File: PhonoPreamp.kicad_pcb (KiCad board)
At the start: 2 copper layers, 100 x 100 mm, 101 parts, among them J1 Conn_01x03, J2 Conn_01x02, J3 Conn_01x02, J4 Conn_01x02, J5 Conn_01x02, J6 Conn_01x01, J7 Conn_01x01, J8 Conn_01x01, J9 Conn_01x01, Q1 2N5551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

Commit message: Made some space around capacitors
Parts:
- moved C26 5.27 mm to (117.2, 110.0)
- moved C15 4.14 mm to (116.2, 45.6)
- moved C25 3.67 mm to (112.7, 110.0)
- moved C16 3.40 mm to (112.0, 45.5)
- moved R39 3.26 mm to (106.0, 41.2)
- moved C12 2.69 mm to (107.5, 45.5)
- moved C24 2.47 mm to (108.2, 110.0)
- moved C13 2.07 mm to (103.2, 45.6)
- moved R40 1.88 mm to (106.2, 105.8)
- moved C14 1.75 mm to (98.7, 45.6)
- moved R36 1.70 mm to (117.0, 119.7)
- moved R35 1.55 mm to (116.7, 122.8)
- moved R33 1.55 mm to (106.8, 122.8)
- moved R34 1.46 mm to (106.8, 119.7)
- moved C23 1.15 mm to (103.8, 110.0)
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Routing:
- net Net-(C12-Pad2): track 29.3 -> 35.4 mm
- net Net-(C22-Pad2): track 30.8 -> 36.2 mm
- net GNDS1: track 148.9 -> 152.7 mm
- net GNDS2: track 239.0 -> 242.1 mm
- net Net-(R39-Pad1): track 30.3 -> 28.6 mm
- net Net-(C28-Pad2): track 21.2 -> 19.7 mm
- net Net-(C15-Pad2): track 8.12 -> 9.35 mm
- net Net-(R40-Pad1): track 115.7 -> 116.8 mm
- net Net-(C29-Pad2): track 19.3 -> 18.6 mm
- net Net-(C25-Pad2): track 8.98 -> 9.49 mm

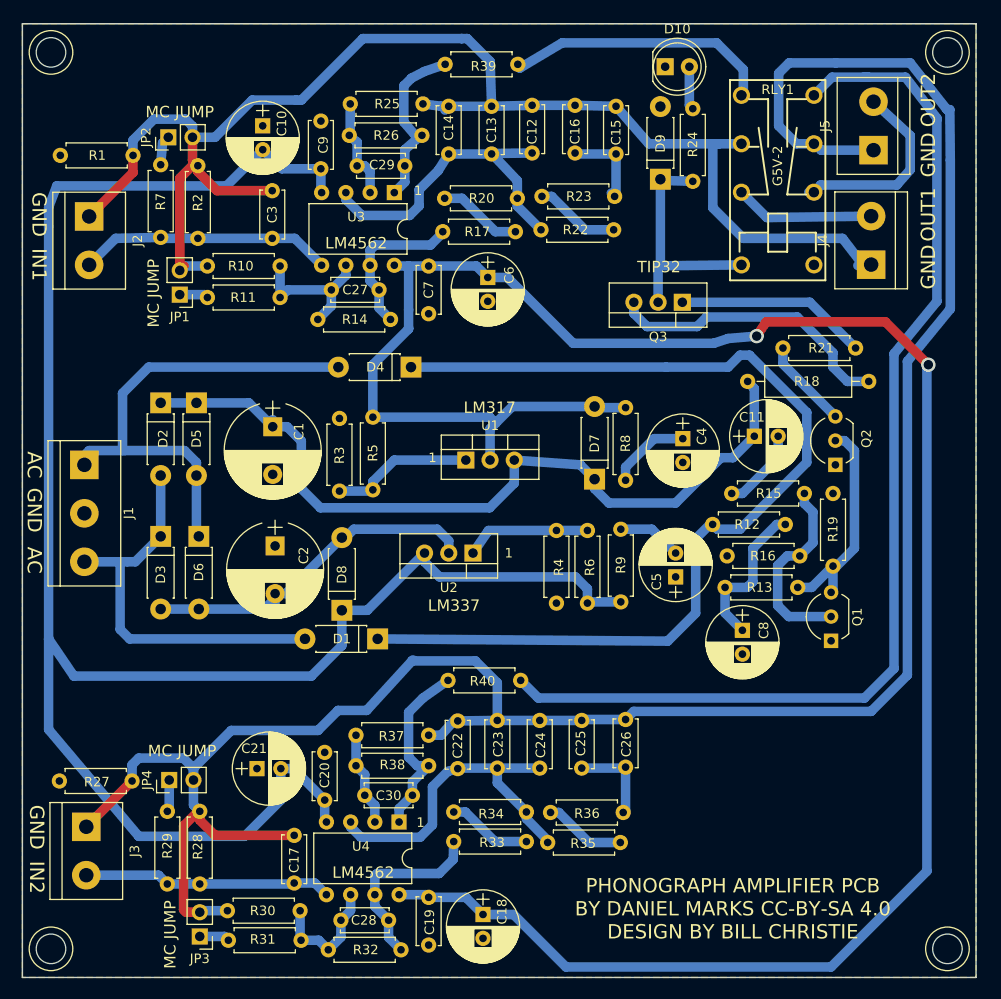
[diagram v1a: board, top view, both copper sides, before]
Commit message: Bigger capacitor footprints
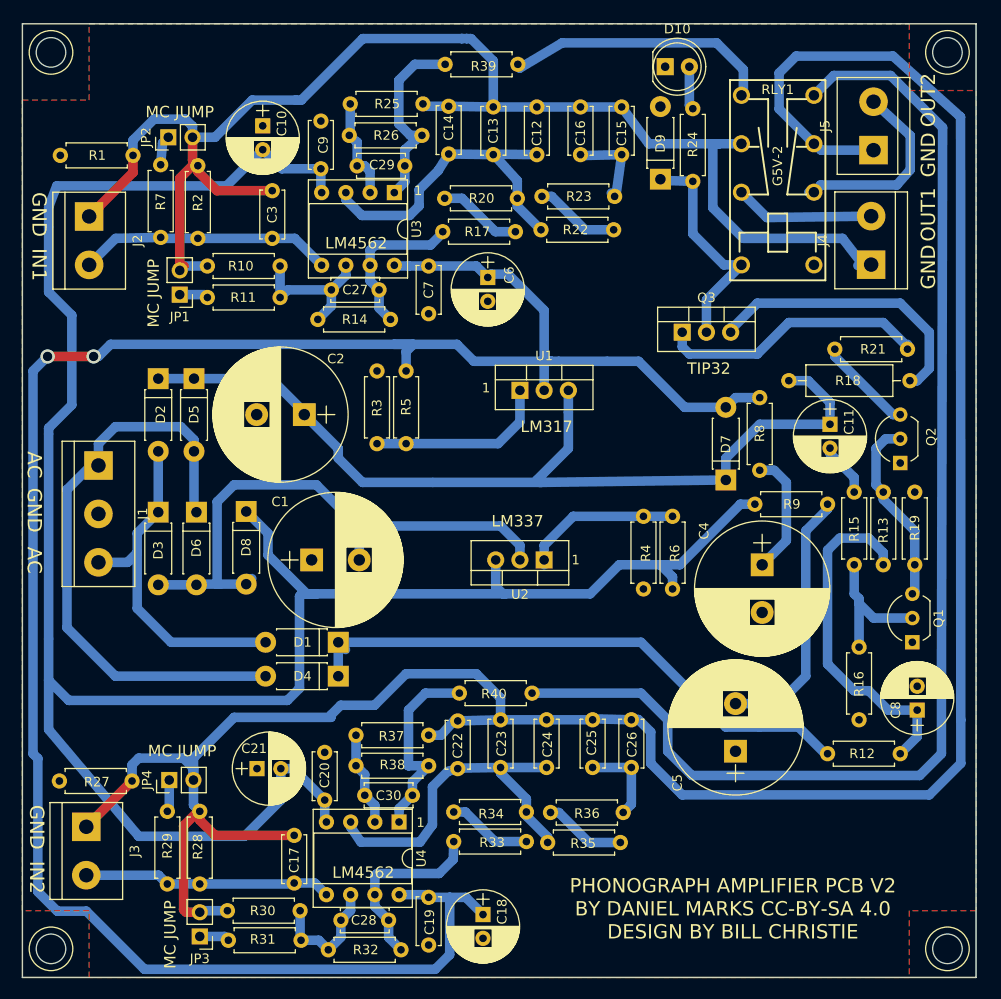
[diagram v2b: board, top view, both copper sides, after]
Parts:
- C1, C2: footprint Capacitors_THT:CP_Radial_D10.0mm_P5.00mm -> Capacitors_THT:CP_Radial_D14.0mm_P5.00mm
- C4, C5: footprint Capacitors_THT:CP_Radial_D7.5mm_P2.50mm -> Capacitors_THT:CP_Radial_D14.0mm_P5.00mm
- U3, U4: footprint Housings_DIP:DIP-8_W7.62mm -> Housings_DIP:DIP-8_W7.62mm_Socket
- moved D4 33.3 mm to (87.1, 105.4)
- moved R12 26.9 mm to (146.1, 113.5)
- moved R16 22.1 mm to (141.7, 110.0), turned to 90 degrees
- moved R9 21.8 mm to (138.4, 87.4), turned to 180 degrees
- moved C8 20.1 mm to (147.8, 109.0), turned to 90 degrees
- moved C5 19.3 mm to (128.8, 113.3)
- moved C4 15.6 mm to (131.6, 93.7)
- moved D8 14.4 mm to (77.5, 88.1), turned to 270 degrees
- moved R8 14.1 mm to (131.3, 76.2)
- moved D7 13.8 mm to (127.8, 84.8)
- moved R13 13.4 mm to (144.3, 86.1), turned to 270 degrees
- moved U1 9.25 mm to (106.2, 75.4)
- moved R4 9.25 mm to (119.1, 96.3)
- moved R15 9.12 mm to (141.2, 93.7), turned to 90 degrees
- moved R6 9.05 mm to (122.2, 96.3)
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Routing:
- net Net-(D1-Pad1): track 107.5 -> 60.8 mm
- net -15V: track 206.5 -> 243.4 mm
- net Net-(C2-Pad2): track 36.8 -> 60.2 mm
- net Net-(C5-Pad2): track 6.79 -> 27.5 mm
- net Net-(C8-Pad1): track 16.9 -> 36.9 mm
- net GNDS2: track 242.1 -> 259.9 mm
- net Net-(R40-Pad1): track 116.8 -> 131.7 mm
- net Net-(C1-Pad1): track 85.5 -> 98.4 mm
- net Net-(D4-Pad2): track 51.1 -> 63.1 mm
- net Net-(Q3-Pad1): track 20.2 -> 28.6 mm
- net Net-(Q1-Pad2): track 20.7 -> 15.1 mm
- net Net-(D1-Pad2): track 42.4 -> 37.2 mm
- net Net-(C4-Pad1): track 8.61 -> 13.0 mm
- net +15V: track 227.0 -> 231.3 mm
- net Net-(R3-Pad1): track 15.4 -> 19.2 mm
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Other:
- board text added: "PHONOGRAPH AMPLIFIER PCB V2 BY DANIEL MARKS CC-BY-SA 4.0 DESIGN BY BILL CHRISTIE"
- board text removed: "PHONOGRAPH AMPLIFIER PCB BY DANIEL MARKS CC-BY-SA 4.0 DESIGN BY BILL CHRISTIE"

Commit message: Added rumble filter
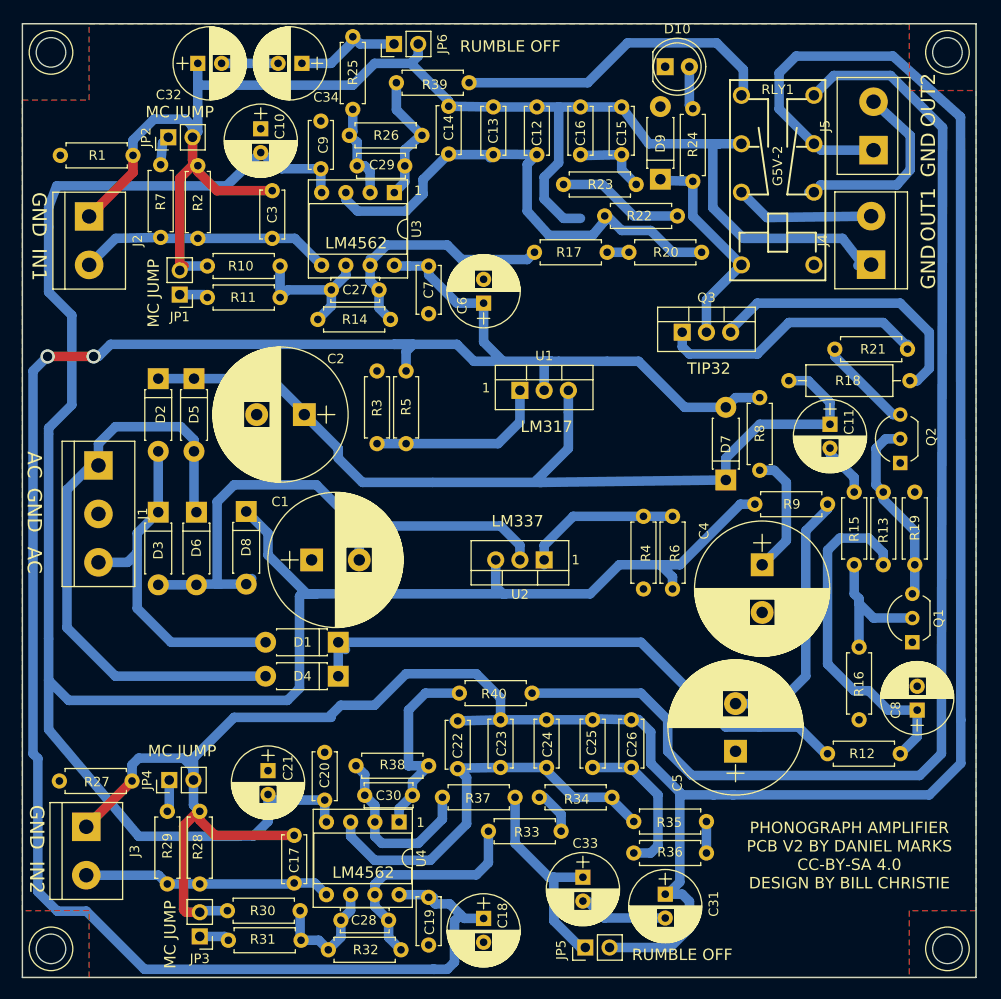
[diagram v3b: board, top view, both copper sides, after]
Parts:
- added C31: 100 uF, Capacitors_THT:CP_Radial_D7.5mm_P2.50mm, F.Cu at (121.4, 128.3)
- added C32: 100 uF, Capacitors_THT:CP_Radial_D7.5mm_P2.50mm, F.Cu at (72.4, 41.1)
- added C33: 100 uF, Capacitors_THT:CP_Radial_D7.5mm_P2.50mm, F.Cu at (112.8, 126.5)
- added C34: 100 uF, Capacitors_THT:CP_Radial_D7.5mm_P2.50mm, F.Cu at (83.3, 41.1)
- added JP5: NO, Pin_Headers:Pin_Header_Straight_1x02_Pitch2.54mm, F.Cu at (113.0, 133.9)
- added JP6: NO, Pin_Headers:Pin_Header_Straight_1x02_Pitch2.54mm, F.Cu at (93.0, 39.1)
- moved R20 20.1 mm to (125.2, 61.0)
- moved R37 11.2 mm to (105.7, 118.1)
- moved R25 10.2 mm to (88.6, 38.4), turned to 270 degrees
- moved R17 9.86 mm to (115.3, 61.0)
- moved R35 9.29 mm to (125.7, 120.7)
- moved R34 9.11 mm to (115.8, 118.1)
- moved R22 6.84 mm to (122.7, 57.1)
- moved R39 5.46 mm to (100.8, 43.2)
- moved R36 4.39 mm to (118.1, 124.0), turned to 0 degrees
- moved R33 3.80 mm to (110.5, 121.7)
- moved C6 2.73 mm to (102.4, 66.3), turned to 90 degrees
- moved R23 2.59 mm to (118.4, 53.8)
- moved C21 1.18 mm to (79.8, 115.3), turned to 270 degrees
- moved C18 0.41 mm to (102.4, 130.8)
- moved C10 0.37 mm to (79.0, 48.0)
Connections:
- R25 pad 1: GNDS1 -> Net-(C34-Pad1)
- R37 pad 1: GNDS2 -> Net-(C33-Pad1)
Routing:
- net GNDS2: track 259.9 -> 282.9 mm
- net Net-(C33-Pad1): track 0.00 -> 22.4 mm
- net Net-(C12-Pad2): track 35.7 -> 53.8 mm
- net Net-(C34-Pad1): track 0.00 -> 11.4 mm
- net GNDS1: track 152.8 -> 162.9 mm
- net Net-(C27-Pad2): track 16.6 -> 26.5 mm
- net Net-(C31-Pad2): track 0.00 -> 9.37 mm
- net Net-(C30-Pad1): track 9.92 -> 18.9 mm
- net Net-(C22-Pad2): track 37.9 -> 45.1 mm
- net Net-(C25-Pad2): track 9.63 -> 16.4 mm
- net Net-(R17-Pad1): track 8.87 -> 2.29 mm
- net Net-(C29-Pad2): track 20.4 -> 14.0 mm
- net Net-(C32-Pad2): track 0.00 -> 5.92 mm
- net Net-(R39-Pad1): track 28.6 -> 34.4 mm
- net Net-(R35-Pad1): track 8.62 -> 3.30 mm
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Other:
- board text added: "RUMBLE OFF"
